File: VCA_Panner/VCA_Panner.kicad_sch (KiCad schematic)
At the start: 79 parts, among them J1 CV1, J2 CV2, J3 Ch1_in, J4 Ch2_in, J5 Ch1_out, J6 Ch2_out, U1 AS3360, U2 TL074, U3 TL074, U4 TL074, U5 LM358

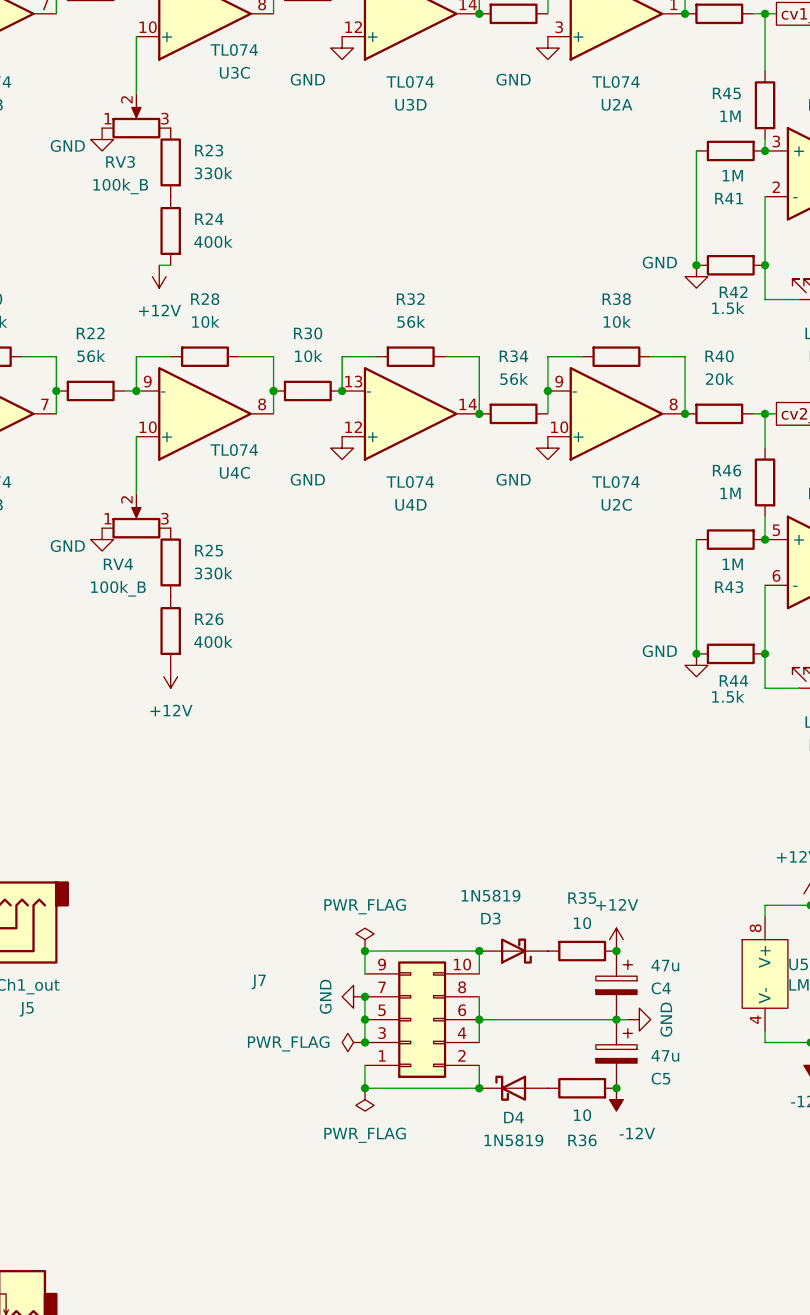
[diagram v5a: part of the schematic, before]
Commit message: Fixed some issues on the vca panner and added teletype beginnings
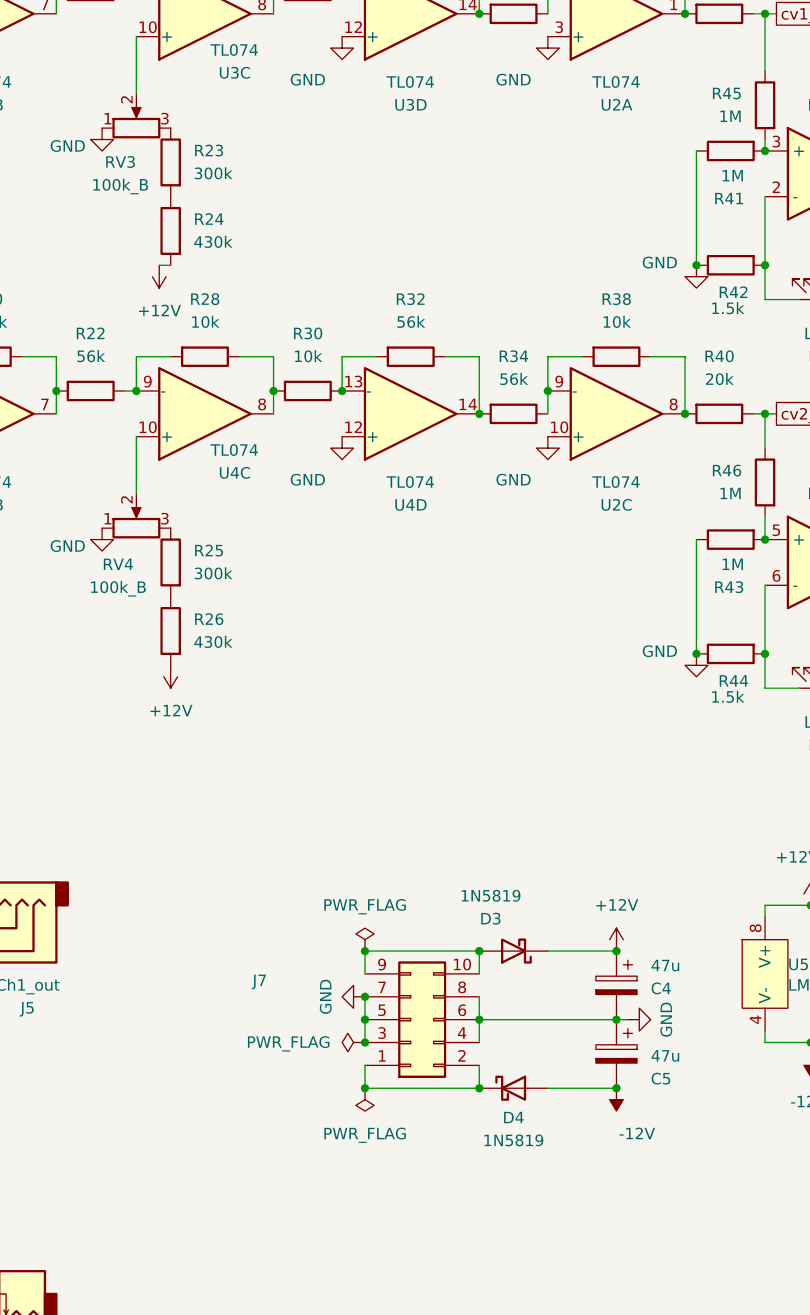
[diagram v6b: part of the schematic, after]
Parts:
- removed R35, R36: 10, Resistor_SMD:R_0805_2012Metric_Pad1.20x1.40mm_HandSolder, symbol Device:R
- R23, R25: value 330k -> 300k
- R24, R26: value 400k -> 430k
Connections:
- net +12V: now also D3.1 (K)
- net -12V: now also D4.2 (A)
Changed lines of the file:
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@@
 	)
 	(junction
-		(at 212.09 139.7)
-		(diameter 0)
-		(color 0 0 0 0)
-	)
-	(junction
 		(at 181.61 33.02)
 		(diameter 0)
@@
 	)
 	(junction
+		(at 212.09 139.7)
+		(diameter 0)
+		(color 0 0 0 0)
+	)
+	(junction
 		(at 219.71 80.01)
 		(diameter 0)
@@
 	(wire
 		(pts
+			(xy 204.47 154.94) (xy 212.09 154.94)
+		)
+		(stroke
+			(width 0)
+			(type default)
+		)
+	)
+	(wire
+		(pts
 			(xy 110.49 41.91) (xy 110.49 38.1)
 		)
@@
 	(wire
 		(pts
+			(xy 204.47 139.7) (xy 212.09 139.7)
+		)
+		(stroke
+			(width 0)
+			(type default)
+		)
+	)
+	(wire
+		(pts
 			(xy 264.16 127) (xy 264.16 140.97)
 		)
@@
 	)
 	(symbol
-		(lib_id "Device:R")
-		(at 208.28 154.94 90)
-		(unit 1)
-		(exclude_from_sim no)
-		(in_bom yes)
-		(on_board yes)
-		(dnp no)
-		(property "Reference" "R36"
-			(at 208.28 160.782 90)
-			(effects
-				(font
-					(size 1.27 1.27)
-				)
-			)
-		)
-		(property "Value" "10"
-			(at 208.28 157.988 90)
-			(effects
-				(font
-					(size 1.27 1.27)
-				)
-			)
-		)
-		(property "Footprint" "Resistor_SMD:R_0805_2012Metric_Pad1.20x1.40mm_HandSolder"
-			(at 208.28 156.718 90)
-			(effects
-				(font
-					(size 1.27 1.27)
-				)
-				(hide yes)
-			)
-		)
-		(property "Datasheet" "~"
-			(at 208.28 154.94 0)
-			(effects
-				(font
-					(size 1.27 1.27)
-				)
-				(hide yes)
-			)
-		)
-		(property "Description" "Resistor"
-			(at 208.28 154.94 0)
-			(effects
-				(font
-					(size 1.27 1.27)
-				)
-				(hide yes)
-			)
-		)
-		(pin "2"
-		)
-		(pin "1"
-		)
-		(instances
-			(project "VCA_Panner"
-				(path "/416439c0-fe9f-449c-a999-c0ea4c6cd459"
-					(reference "R36")
-					(unit 1)
-				)
-			)
-		)
-	)
-	(symbol
 		(lib_id "power:GND")
 		(at 83.82 96.52 0)
@@
 	)
 	(symbol
-		(lib_id "Device:R")
-		(at 208.28 139.7 270)
-		(unit 1)
-		(exclude_from_sim no)
-		(in_bom yes)
-		(on_board yes)
-		(dnp no)
-		(property "Reference" "R35"
-			(at 208.28 133.858 90)
-			(effects
-				(font
-					(size 1.27 1.27)
-				)
-			)
-		)
-		(property "Value" "10"
-			(at 208.28 136.652 90)
-			(effects
-				(font
-					(size 1.27 1.27)
-				)
-			)
-		)
-		(property "Footprint" "Resistor_SMD:R_0805_2012Metric_Pad1.20x1.40mm_HandSolder"
-			(at 208.28 137.922 90)
-			(effects
-				(font
-					(size 1.27 1.27)
-				)
-				(hide yes)
-			)
-		)
-		(property "Datasheet" "~"
-			(at 208.28 139.7 0)
-			(effects
-				(font
-					(size 1.27 1.27)
-				)
-				(hide yes)
-			)
-		)
-		(property "Description" "Resistor"
-			(at 208.28 139.7 0)
-			(effects
-				(font
-					(size 1.27 1.27)
-				)
-				(hide yes)
-			)
-		)
-		(pin "2"
-		)
-		(pin "1"
-		)
-		(instances
-			(project "VCA_Panner"
-				(path "/416439c0-fe9f-449c-a999-c0ea4c6cd459"
-					(reference "R35")
-					(unit 1)
-				)
-			)
-		)
-	)
-	(symbol
 		(lib_id "Device:C")
 		(at 121.92 142.24 180)
@@
 			)
 		)
-		(property "Value" "400k"
+		(property "Value" "430k"
 			(at 165.1 60.9599 0)
 			(effects
@@
 			)
 		)
-		(property "Value" "330k"
+		(property "Value" "300k"
 			(at 165.1 97.7899 0)
 			(effects
@@
 			)
 		)
-		(property "Value" "330k"
+		(property "Value" "300k"
 			(at 165.1 53.3399 0)
 			(effects
@@
 			)
 		)
-		(property "Value" "400k"
+		(property "Value" "430k"
 			(at 165.1 105.4099 0)
 			(effects
